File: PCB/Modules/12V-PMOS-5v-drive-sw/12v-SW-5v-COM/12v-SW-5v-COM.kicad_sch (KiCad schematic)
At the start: 2 parts, among them J1 Screw_Terminal_01x02

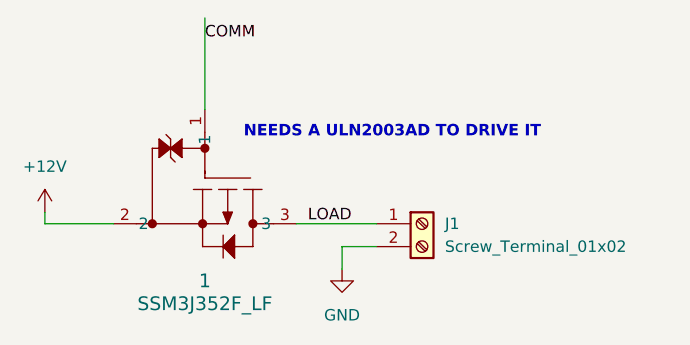
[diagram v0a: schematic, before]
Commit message: Added switch modules and RS485 module
Signed-off-by: Simonca Raul <simonca.raul@gmail.com>
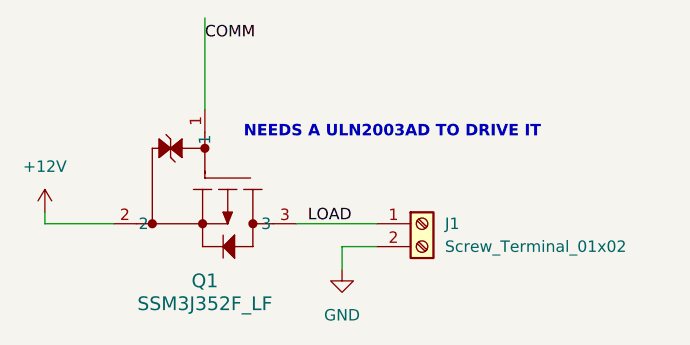
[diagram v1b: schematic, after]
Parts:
- J1: footprint TerminalBlock:TerminalBlock_Xinya_XY308-2.54-2P_1x02_P2.54mm_Horizontal -> TerminalBlock:TerminalBlock_bornier-2_P5.08mm
- Q1: renamed from 1; footprint (none) -> Package_S-Mini:S-MINI_TOS
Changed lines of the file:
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@@
 			)
 		)
-		(property "Footprint" "TerminalBlock:TerminalBlock_Xinya_XY308-2.54-2P_1x02_P2.54mm_Horizontal"
+		(property "Footprint" "TerminalBlock:TerminalBlock_bornier-2_P5.08mm"
 			(at 173.99 69.85 0)
 			(effects
@@
 		(dnp no)
 		(fields_autoplaced yes)
-		(property "Reference" "1"
+		(property "Reference" "Q1"
 			(at 149.86 76.2 90)
 			(effects
@@
 			)
 		)
-		(property "Footprint" ""
+		(property "Footprint" "Package_S-Mini:S-MINI_TOS"
 			(at 157.48 59.69 0)
 			(effects
@@
 			(project ""
 				(path "/ff6dfdf3-1cbb-4288-8f19-32c918aa735a"
-					(reference "1")
+					(reference "Q1")
 					(unit 1)
 				)
